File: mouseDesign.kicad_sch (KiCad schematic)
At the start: 37 parts, among them J1 USB_C_Receptacle, J2 JST_CONN, Q2 AO8810, U1 MCP1700T-2502E-MB, U2 BQ24090DGQ, U3 USBLC6-2SC6, U4 DW01A

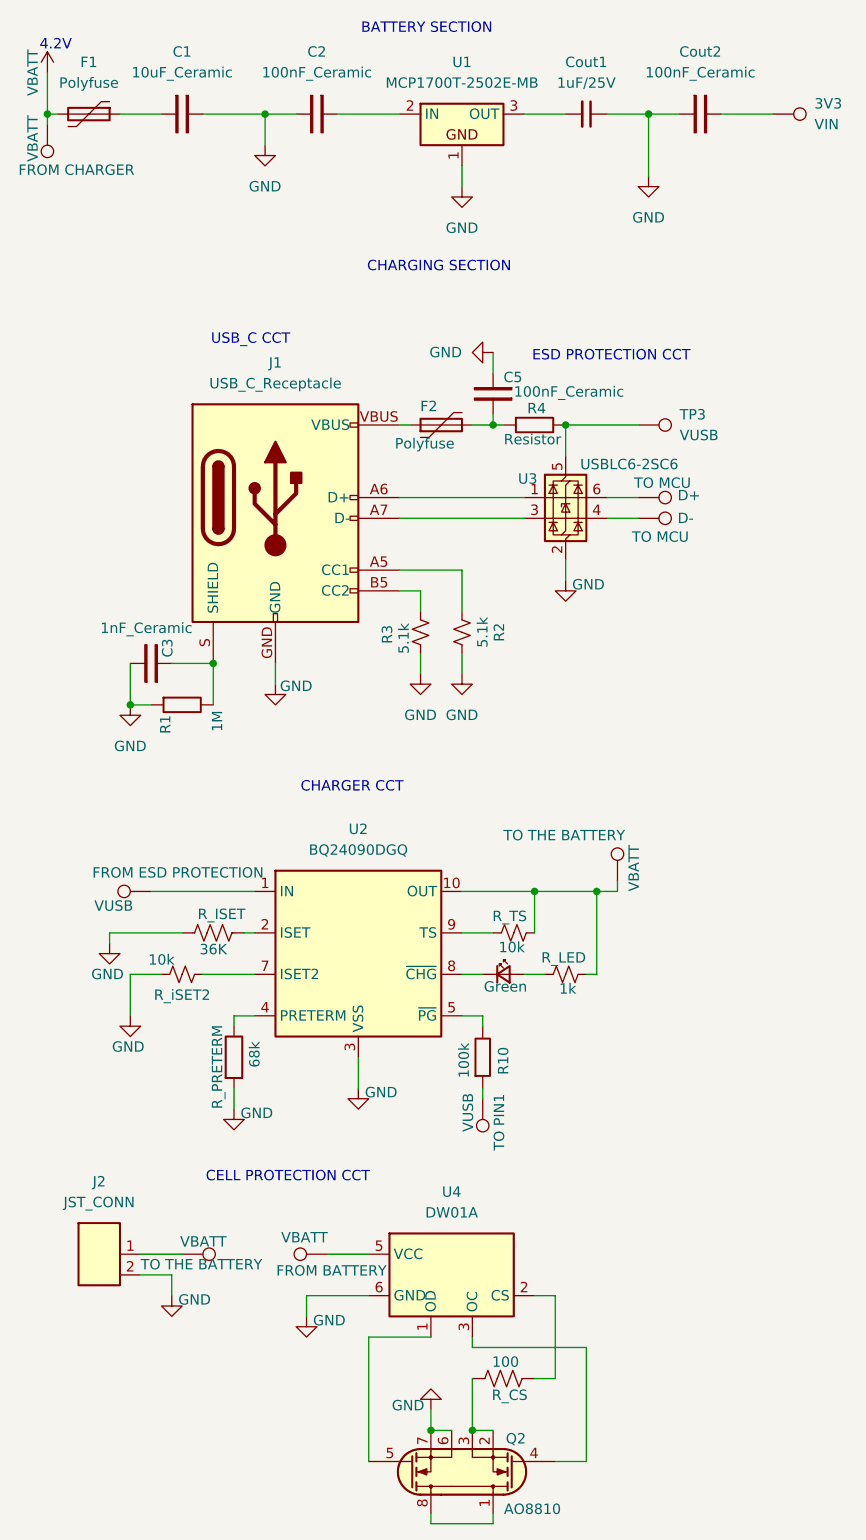
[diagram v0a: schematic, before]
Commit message: Updated final power system design and gitignore
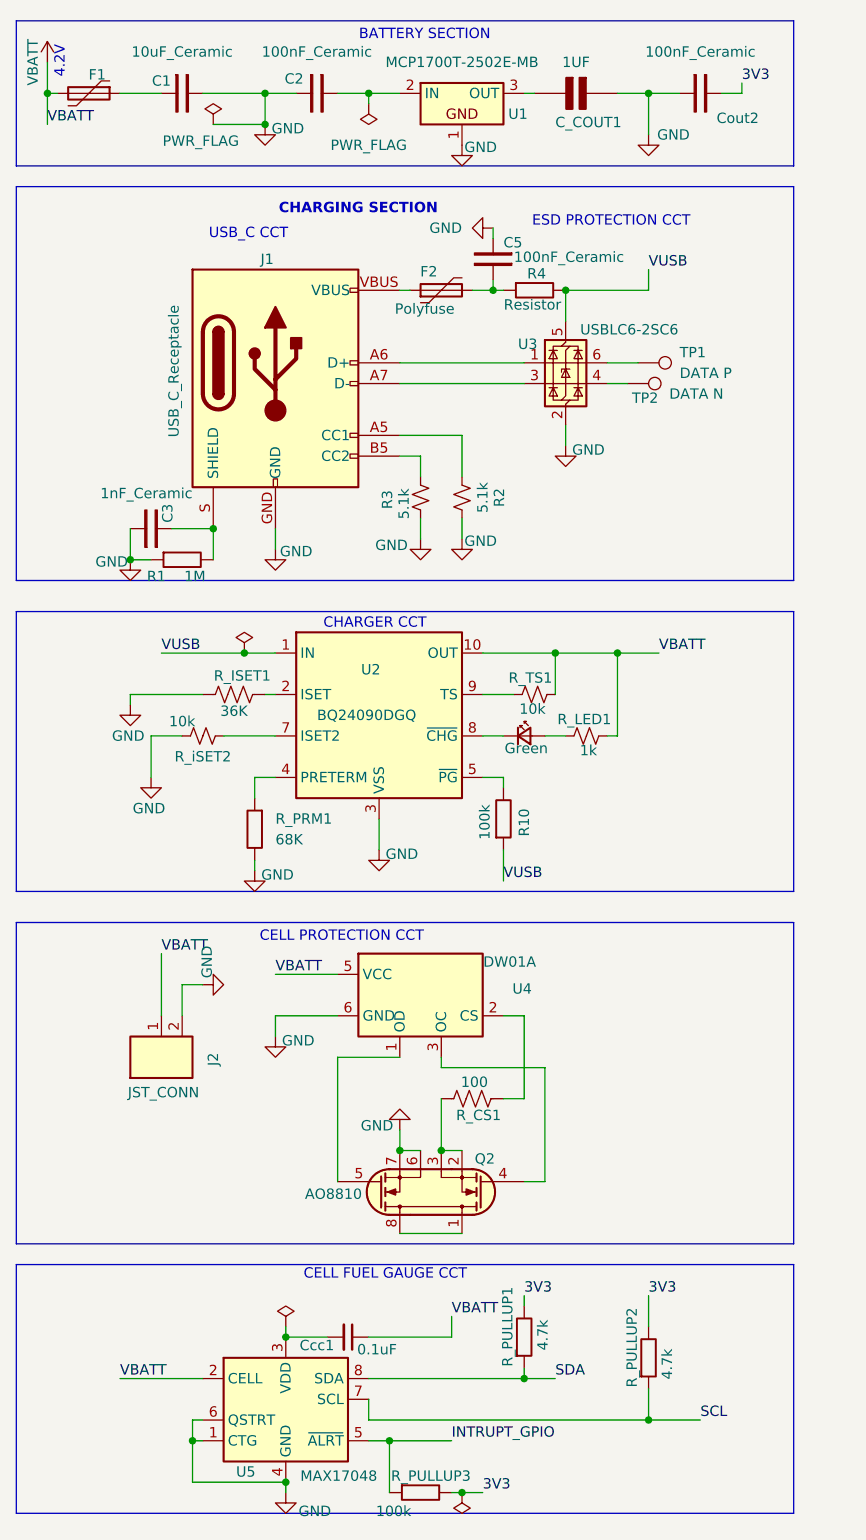
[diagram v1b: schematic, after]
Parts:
- removed 3V3: VIN, 4ms_Capacitor:C_0603, symbol Connector:TestPoint
- removed Cout1: 1uF_0603_25V, 4ms_Capacitor:C_0603, symbol PCM_4ms_Capacitor:1uF_0603_25V
- removed D+, D-: TO MCU, Module:Maple_Mini, symbol Connector:TestPoint
- removed R_PRETERM: 68k_0603, 4ms_Resistor:R_0603, symbol PCM_4ms_Resistor:68k_0603
- removed TP3: VUSB, PCM_Package_SO_AKL:TSSOP-8_4.4x3mm_P0.65mm, symbol Connector:TestPoint
- removed VBATT: TO THE BATTERY, Module:Maple_Mini, symbol Connector:TestPoint
- removed VBATT: FROM BATTERY, symbol Connector:TestPoint
- removed VBATT: FROM CHARGER, symbol Connector:TestPoint
- removed VBATT: TO THE BATTERY, PCM_Package_SO_AKL:TSSOP-8_4.4x3mm_P0.65mm, symbol Connector:TestPoint
- removed VUSB: FROM ESD PROTECTION, PCM_Package_SO_AKL:TSSOP-8_4.4x3mm_P0.65mm, symbol Connector:TestPoint
- removed VUSB: TO PIN1, PCM_Package_SO_AKL:TSSOP-8_4.4x3mm_P0.65mm, symbol Connector:TestPoint
- added C_COUT1: 1UF, Resistor_THT:R_Axial_DIN0207_L6.3mm_D2.5mm_P10.16mm_Horizontal, symbol PCM_Elektuur:C
- added Ccc1: 0.1uF_0805_50V, PCM_4ms_Capacitor:C_0805, symbol PCM_4ms_Capacitor:0.1uF_0805_50V
- added R_PRM1: 68K, Resistor_THT:R_Axial_DIN0207_L6.3mm_D2.5mm_P10.16mm_Horizontal, symbol PCM_SL_Devices:Resistor
- added R_PULLUP1, R_PULLUP2: 4.7k, Resistor_THT:R_Axial_DIN0207_L6.3mm_D2.5mm_P10.16mm_Horizontal, symbol PCM_SL_Resistors:100k
- added R_PULLUP3: 100k, Resistor_THT:R_Axial_DIN0207_L6.3mm_D2.5mm_P10.16mm_Horizontal, symbol PCM_SL_Resistors:100k
- added TP1: DATA P, symbol Connector:TestPoint
- added TP2: DATA N, symbol Connector:TestPoint
- added U5: MAX17048, PCM_SparkFun-Semiconductor-Standard:DFN-8_2x2mm_P0.5mm_EP1.2x0.8mm, symbol PCM_SparkFun-IC-Power:MAX17048
- F2: footprint PCM_SparkFun-Connector:USB-C_16 -> Fuse:Fuse_Bourns_MF-RG300
- renumbered R_CS to R_CS1, R_ISET to R_ISET1, R_LED to R_LED1, R_TS to R_TS1
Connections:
- net GND: now also C_COUT1.1 (+), R_PRM1.2, U5.1 (CTG), U5.4 (GND), U5.6 (QSTRT), U5.9 (GND)
- net VBATT: now also J2.1, R_LED1.2, R_TS1.2, U2.10 (OUT), U4.5 (VCC), Ccc1.1, U5.2 (CELL)
- net VUSB: now reaches U2.1 (IN)
- net VUSB: now also R10.1, R4.2, U3.5 (VBUS)
- net at U2.4 (PRETERM): now also R_PRM1.1
- net at U3.4 (I/O2): now also TP2.1
- net at U3.6 (I/O1): now also TP1.1
- net 3V3: now reaches Cout2.2
- net 3V3: now also R_PULLUP1.2, R_PULLUP2.2, R_PULLUP3.2
- net at U1.3 (OUT): now also C_COUT1.2 (-)
- new net: Ccc1.2, U5.3 (VDD)
- new net INTRUPT_GPIO: R_PULLUP3.1, U5.5 (~{ALRT})
- new net SCL: R_PULLUP2.1, U5.7 (SCL)
- new net SDA: R_PULLUP1.1, U5.8 (SDA)
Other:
- note added: "CELL FUEL GAUGE CCT"
- moved on the sheet: C1, C2, C3, C5, Cout2, F1, F2, J1, J2, Q2, R1, R10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

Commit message: Added MCU
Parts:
- added C10, C11, C12, C4, C6, C7, C8, C9: 100nF, symbol PCM_Elektuur:C
- added U6: nRF52840, Package_DFN_QFN:Nordic_AQFN-73-1EP_7x7mm_P0.5mm, symbol MCU_Nordic:nRF52840
- added U7: PMW3360DM-T2QU, openinput:PXI-DIP-16, symbol PCM_openinput:PMW3360DM-T2QU
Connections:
- net GND: now also C10.2 (-), C4.2 (-), C6.2 (-), C7.2 (-), C8.2 (-), C9.2 (-)
- new net: C4.1 (+), U6.A18 (DEC2)
- new net: C9.1 (+), U6.E24 (DEC6)
- new net: C7.1 (+), U6.B5 (DEC4)
- new net: C8.1 (+), U6.N24 (DEC5)
- new net: C10.1 (+), U6.C1 (DEC1)
- new net: U6.A22 (VDD), U6.AD14 (VDD), U6.AD23 (VDD), U6.B1 (VDD), U6.W1 (VDD)
- new net: U6.B7 (VSS), U6.EP (VSS)
- new net: C6.1 (+), U6.D23 (DEC3)

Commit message: MCU Progress
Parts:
- removed TP1: DATA P, symbol Connector:TestPoint
- removed TP2: DATA N, symbol Connector:TestPoint
- added C13: 100nF, symbol PCM_Elektuur:C
- added R5: 4.7k, PCM_SparkFun-Resistor:R_0603_1608Metric, symbol PCM_SparkFun-Resistor:R
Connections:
- net 3V3: now also C11.2 (-), C12.1 (+), U6.A22 (VDD), U6.AD14 (VDD), U6.AD23 (VDD), U6.B1 (VDD), U6.W1 (VDD), U6.Y2 (VDDH)
- net GND: now also C11.1 (+), C12.2 (-), U6.B7 (VSS), U6.EP (VSS), C13.1 (+), R5.1
- net VUSB: now also U6.AD2 (VBUS)
- net DATA_P: now reaches U3.6 (I/O1)
- net DATA_P: now also U6.AD6 (D+)
- net DATA_N: now reaches U3.4 (I/O2)
- net DATA_N: now also U6.AD4 (D-)
- net at U6.AC5 (DECUSB): now also C13.2 (-), R5.2
- net GND1-RF: now reaches U6.F23 (VSS_PA)
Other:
- moved on the sheet: C10, C11, C12, C4, C6, C7, C8, C9, U6
